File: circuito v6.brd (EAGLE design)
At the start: 90.5 x 59.5 mm, 64 parts, among them IC1 LM324N

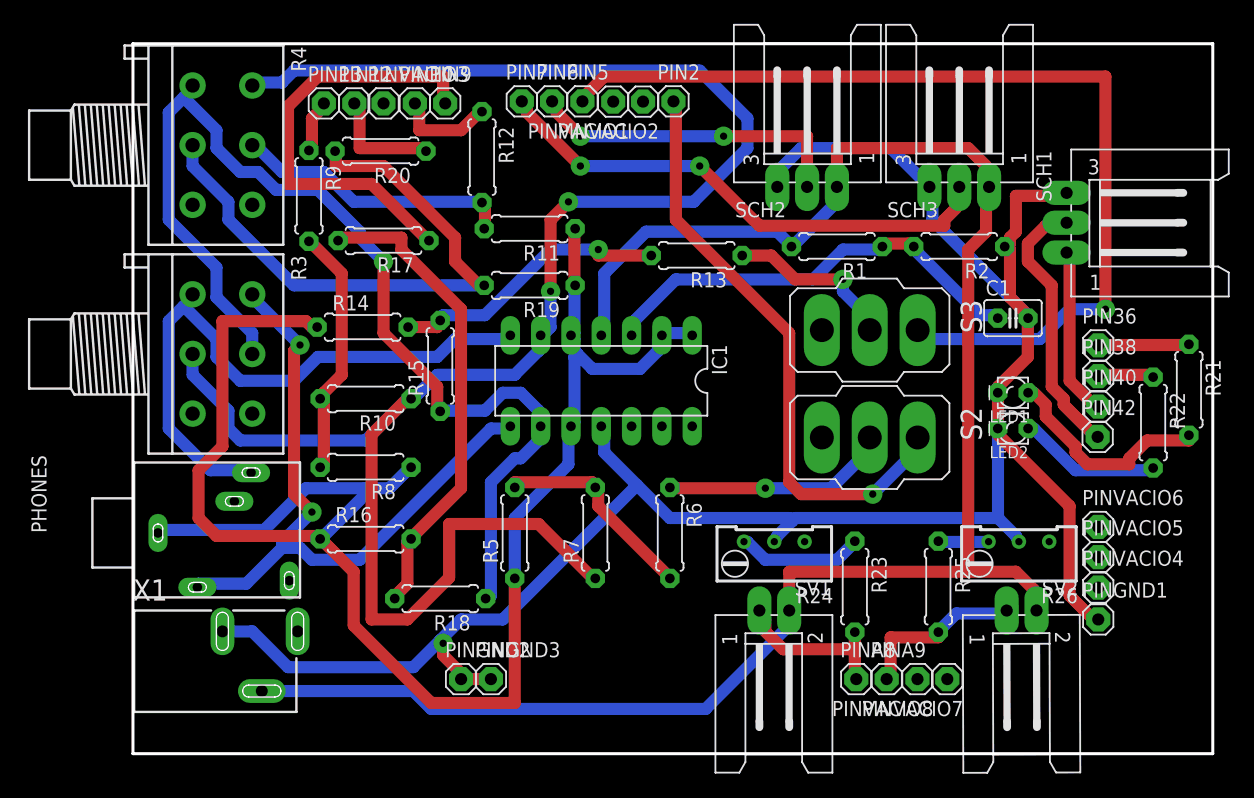
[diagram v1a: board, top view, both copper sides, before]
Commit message: Cambio de pines
Tras chequear lado izq y der de los phones, cambio los nombres de los pines para que queden
Estimulo Izq PIN 11
Estimulo Der PIN 12
Feedback Izq PIN 2
Feedback Der PIN 5
Ruido blanco Izq PIN 9
Ruido blanco Der PIN 10

Se reacomodan los pins, despues de renombrarlos, en sus posiciones correctas.
Se ripupea todo el routeo hecho.

Se creo esta branch porque eliminar los commits que se realizaron con estos mismos cambios pero no exitosamente, es no-trivial.
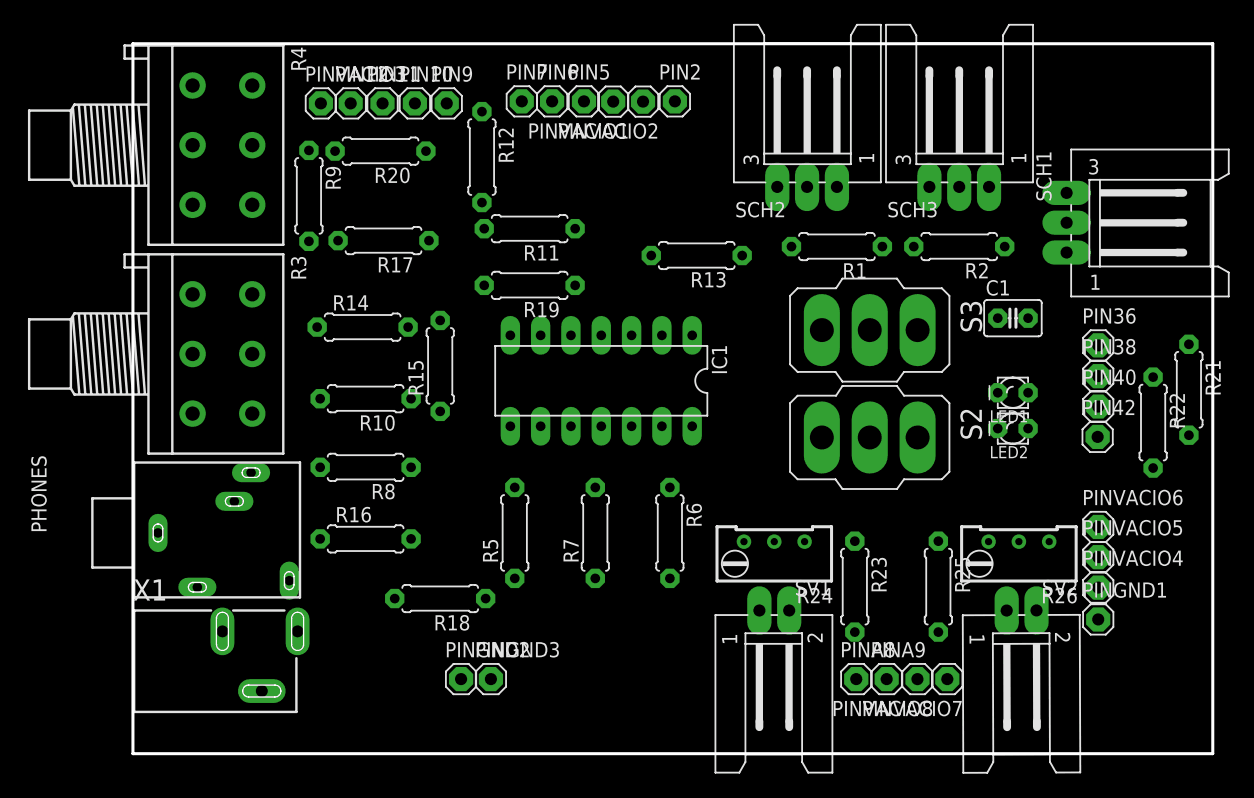
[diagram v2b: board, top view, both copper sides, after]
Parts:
- removed PIN13: (no value), pinhead:1X01
- added PIN11: (no value), pinhead:1X01
- moved PINVACIO3 5.25 mm to (28.8, 50.8)
- moved PIN12 0.30 mm to (31.2, 50.8)
- moved PIN5 0.13 mm to (50.8, 50.9)
- moved PIN9 0.13 mm to (39.3, 50.8)
- moved PIN2 0.12 mm to (58.4, 50.9)
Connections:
- net N$16: now also PIN2.1; no longer PIN5.1
- net N$20: now also PIN11.1; no longer PIN9.1
- net N$21: now also PIN9.1; no longer PIN12.1
- net N$3: now also PIN12.1; no longer PIN13.1
- net N$7: now also PIN5.1; no longer PIN2.1
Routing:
- net GND: track 175.7 -> 0.00 mm, vias 1 -> 0
- net N$4: track 160.4 -> 0.00 mm, vias 2 -> 0
- net VCC: track 156.0 -> 0.00 mm
- net N$8: track 144.8 -> 0.00 mm
- net N$13: track 92.0 -> 0.00 mm, vias 1 -> 0
- net N$16: track 81.5 -> 0.00 mm, vias 1 -> 0
- net N$30: track 57.5 -> 0.00 mm, vias 2 -> 0
- net N$37: track 53.0 -> 0.00 mm
- net N$18: track 50.2 -> 0.00 mm
- net N$7: track 49.6 -> 0.00 mm, vias 1 -> 0
- net N$28: track 43.8 -> 0.00 mm, vias 2 -> 0
- net N$19: track 40.0 -> 0.00 mm
- net N$1: track 37.1 -> 0.00 mm
- net N$20: track 36.6 -> 0.00 mm
- net N$29: track 27.1 -> 0.00 mm, vias 2 -> 0
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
